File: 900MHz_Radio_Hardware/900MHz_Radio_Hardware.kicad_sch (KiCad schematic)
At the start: 10 parts, among them U1 TSR_1-2450

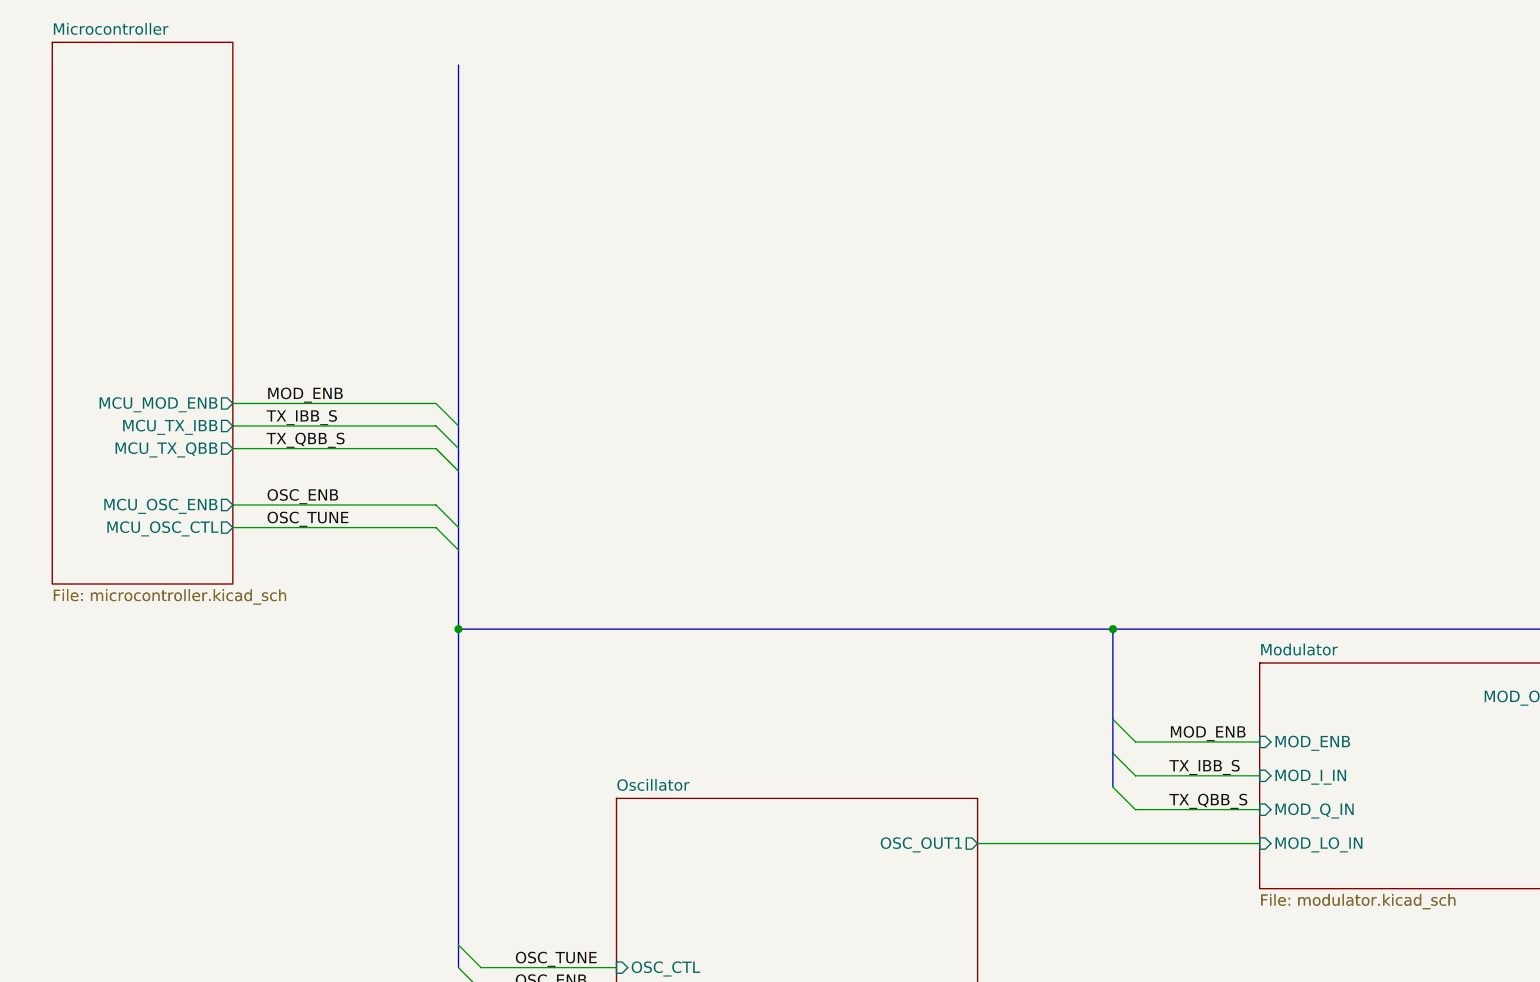
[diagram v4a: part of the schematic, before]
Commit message: Replaced DAC
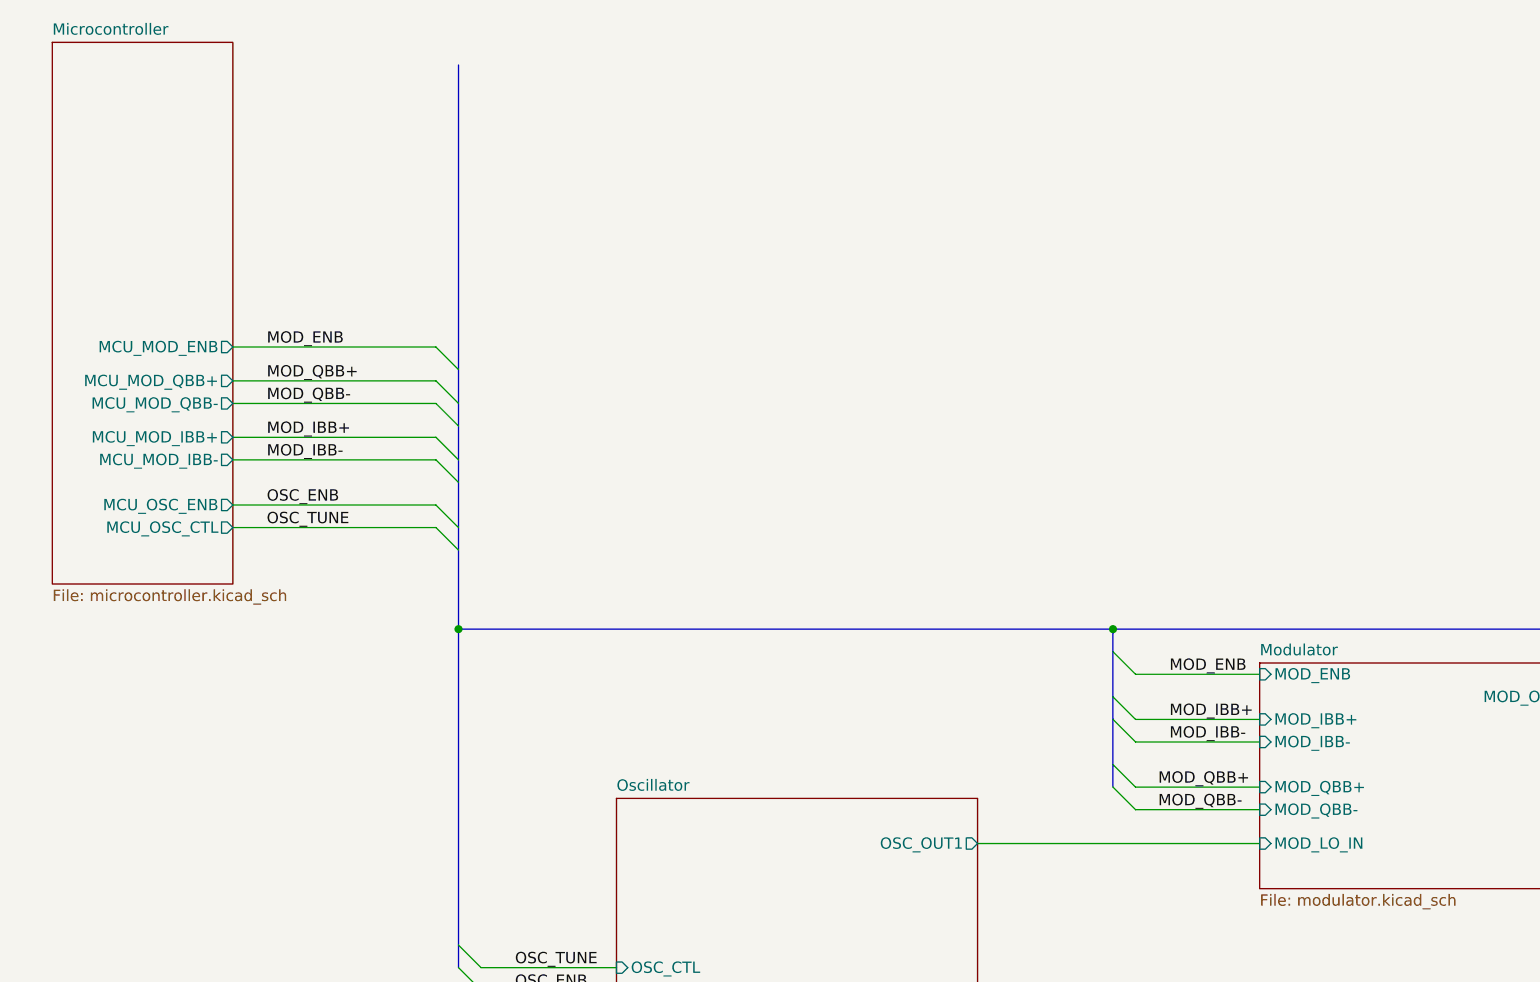
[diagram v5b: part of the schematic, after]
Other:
- sheet Microcontroller ports: added MCU_MOD_IBB+, MCU_MOD_IBB-, MCU_MOD_QBB+, MCU_MOD_QBB-; removed MCU_TX_IBB, MCU_TX_QBB
- sheet Modulator ports: added MOD_IBB+, MOD_IBB-, MOD_QBB+, MOD_QBB-; removed MOD_I_IN, MOD_Q_IN

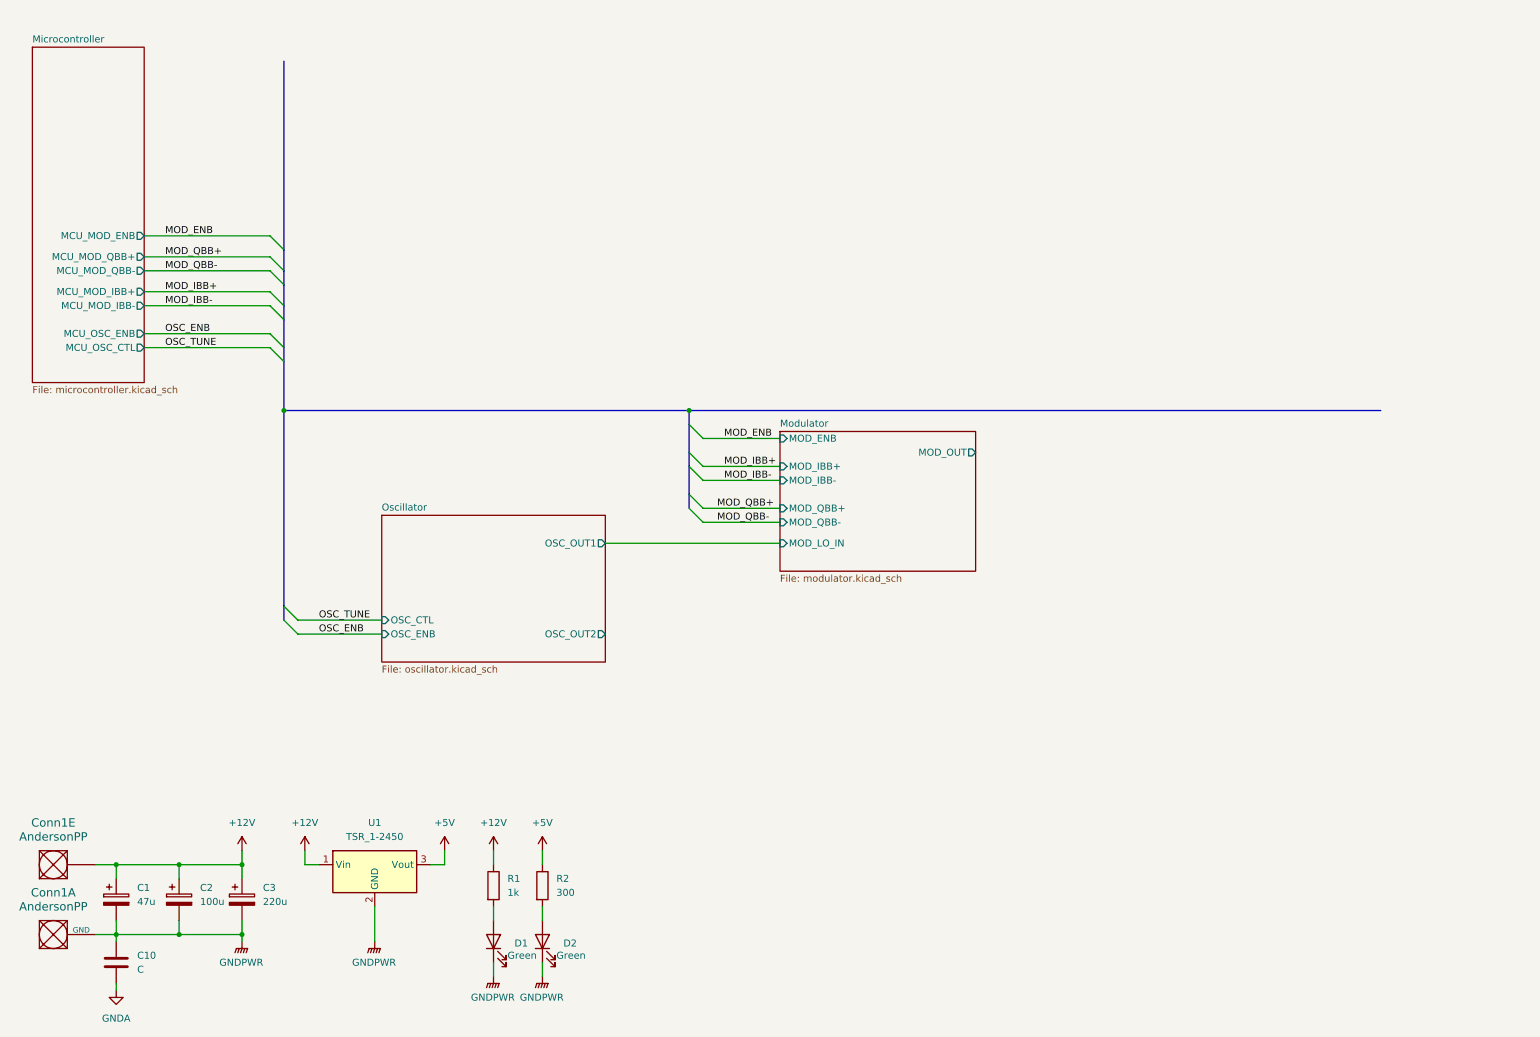
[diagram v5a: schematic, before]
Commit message: Started demodulator
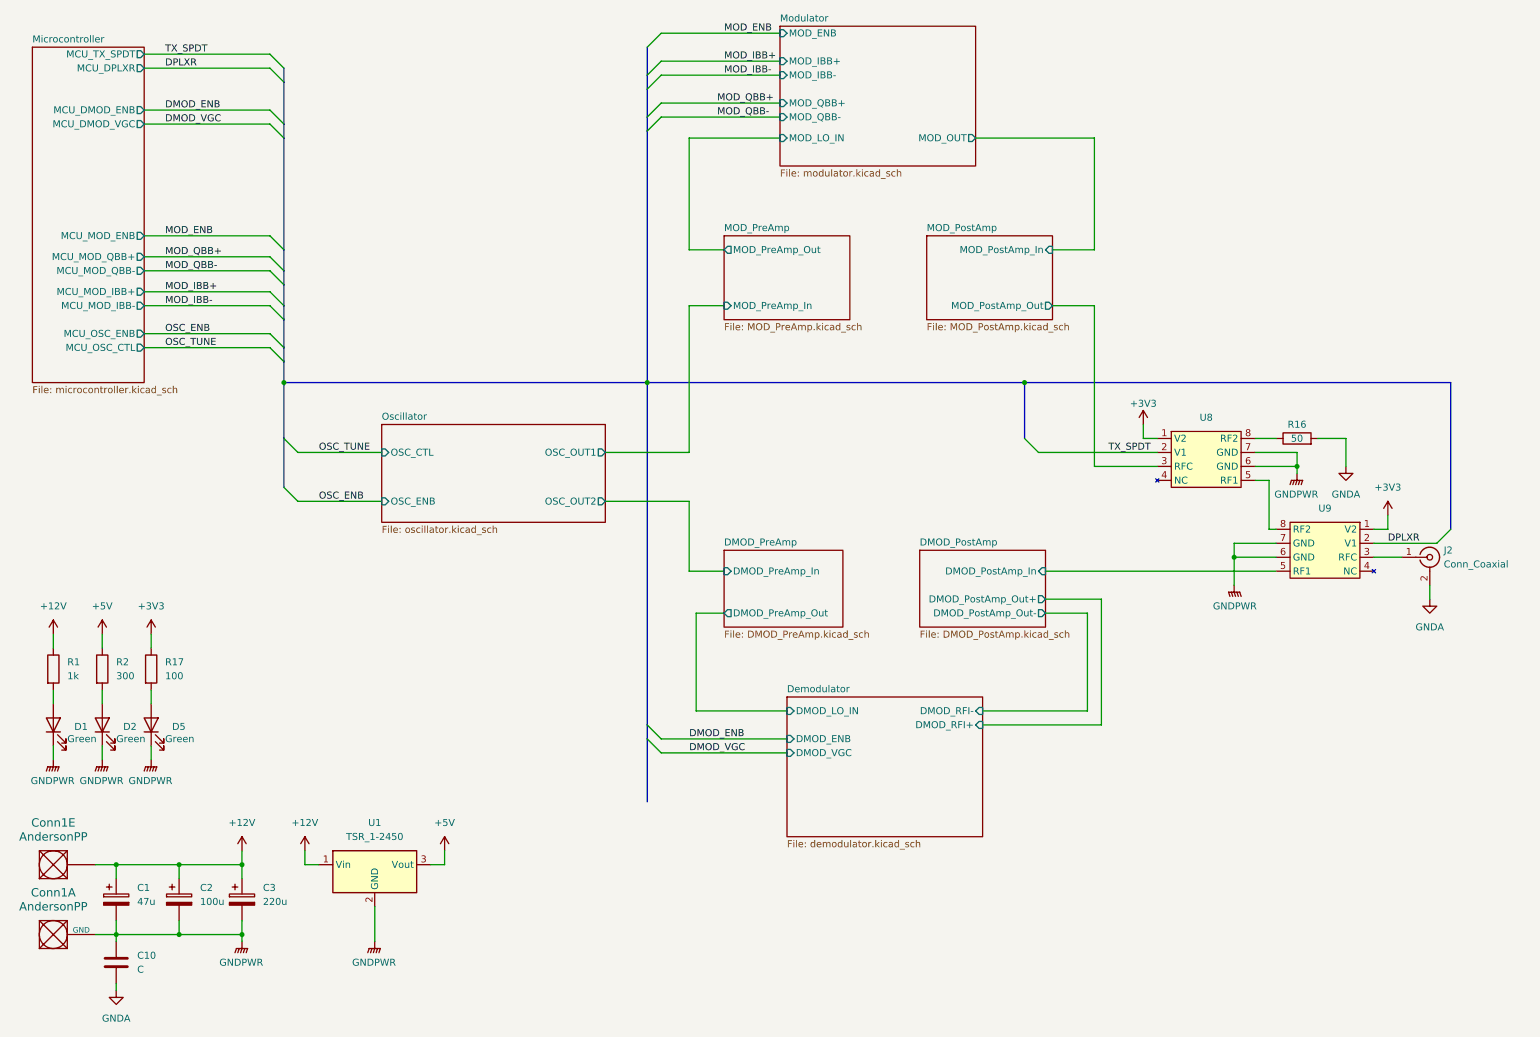
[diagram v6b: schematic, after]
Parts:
- added D5: Green, symbol Device:LED
- added J2: Conn_Coaxial, symbol Connector:Conn_Coaxial
- added R16: 50, symbol Device:R
- added R17: 100, symbol Device:R
- added U8, U9: ~, Package_SO:MSOP-8-1EP_3x3mm_P0.65mm_EP1.73x1.85mm, symbol MRDT_ICs:PE4251
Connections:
- net GNDA: now also J2.2 (Ext), R16.2
- net GNDPWR: now also D5.1 (K), U8.6 (GND), U8.7 (GND), U9.6 (GND), U9.7 (GND)
- new net: D5.2 (A), R17.2
- new net: J2.1 (In), U9.3 (RFC)
- new net: U8.5 (RF1), U9.8 (RF2)
- new net: R16.1, U8.8 (RF2)
- new net +3V3: R17.1, U8.1 (V2), U9.1 (V2)
- new net DMOD_PostAmp/DMOD_PostAmp_In: U9.5 (RF1)
- new net DPLXR: U9.2 (V1)
- new net MOD_PostAmp/MOD_PostAmp_Out: U8.3 (RFC)
- new net TX_SPDT: U8.2 (V1)
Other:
- added sheet DMOD_PostAmp (DMOD_PostAmp.kicad_sch)
- added sheet DMOD_PreAmp (DMOD_PreAmp.kicad_sch)
- added sheet Demodulator (demodulator.kicad_sch)
- added sheet MOD_PostAmp (MOD_PostAmp.kicad_sch)
- added sheet MOD_PreAmp (MOD_PreAmp.kicad_sch)
- sheet Microcontroller ports: added MCU_DMOD_ENB, MCU_DMOD_VGC, MCU_DPLXR, MCU_TX_SPDT; removed none
- moved on the sheet: D1, D2, R1, R2

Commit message: Worked on demodulator
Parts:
- removed C10: C, symbol Device:C
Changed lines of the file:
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@@
-    )
-  )
-  (symbol (lib_id "Device:C") (at 30.48 185.42 0) (unit 1)
-    (in_bom yes) (on_board yes) (dnp no) (fields_autoplaced)
-    (property "Reference" "C10" (at 34.29 184.15 0)
-      (effects (font (size 1.27 1.27)) (justify left))
-    )
-    (property "Value" "C" (at 34.29 186.69 0)
-      (effects (font (size 1.27 1.27)) (justify left))
-    )
-    (property "Footprint" "" (at 31.4452 189.23 0)
-      (effects (font (size 1.27 1.27)) hide)
-    )
-    (property "Datasheet" "~" (at 30.48 185.42 0)
-      (effects (font (size 1.27 1.27)) hide)
-    )
-    (pin "1")
-    (pin "2")
-    (instances
-      (project "900MHz_Radio_Hardware"
-        (path "/8d477a51-3dbb-4c04-84c7-90186d141eda"
-          (reference "C10") (unit 1)
-        )
-      )
     )
   )

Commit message: Renamed amp sheets
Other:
- sheet DMOD_PostAmp renamed DMOD_RF_Amp
- sheet DMOD_PreAmp renamed DMOD_LO_Amp
- sheet MOD_PostAmp renamed MOD_RF_Amp
- sheet MOD_PreAmp renamed MOD_LO_Amp
- sheet DMOD_LO_Amp: file DMOD_PreAmp.kicad_sch -> DMOD_LO_Amp.kicad_sch
- sheet DMOD_RF_Amp: file DMOD_PostAmp.kicad_sch -> DMOD_RF_Amp.kicad_sch
- sheet MOD_LO_Amp: file MOD_PreAmp.kicad_sch -> MOD_LO_Amp.kicad_sch
- sheet MOD_RF_Amp: file MOD_PostAmp.kicad_sch -> MOD_RF_Amp.kicad_sch
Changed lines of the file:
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@@
     (stroke (width 0.1524) (type solid))
     (fill (color 0 0 0 0.0000))
-    (property "Sheetname" "MOD_PostAmp" (at 177.8 52.6284 0)
+    (property "Sheetname" "MOD_RF_Amp" (at 177.8 52.6284 0)
       (effects (font (size 1.27 1.27)) (justify left bottom))
     )
-    (property "Sheetfile" "MOD_PostAmp.kicad_sch" (at 177.8 69.1646 0)
+    (property "Sheetfile" "MOD_RF_Amp.kicad_sch" (at 177.8 69.1646 0)
       (effects (font (size 1.27 1.27)) (justify left top))
     )
@@
     (stroke (width 0.1524) (type solid))
     (fill (color 0 0 0 0.0000))
-    (property "Sheetname" "MOD_PreAmp" (at 140.97 52.6284 0)
+    (property "Sheetname" "MOD_LO_Amp" (at 140.97 52.6284 0)
       (effects (font (size 1.27 1.27)) (justify left bottom))
     )
-    (property "Sheetfile" "MOD_PreAmp.kicad_sch" (at 140.97 69.1646 0)
+    (property "Sheetfile" "MOD_LO_Amp.kicad_sch" (at 140.97 69.1646 0)
       (effects (font (size 1.27 1.27)) (justify left top))
     )
@@
     (stroke (width 0.1524) (type solid))
     (fill (color 0 0 0 0.0000))
-    (property "Sheetname" "DMOD_PostAmp" (at 176.53 109.7784 0)
+    (property "Sheetname" "DMOD_RF_Amp" (at 176.53 109.7784 0)
       (effects (font (size 1.27 1.27)) (justify left bottom))
     )
-    (property "Sheetfile" "DMOD_PostAmp.kicad_sch" (at 176.53 125.0446 0)
+    (property "Sheetfile" "DMOD_RF_Amp.kicad_sch" (at 176.53 125.0446 0)
       (effects (font (size 1.27 1.27)) (justify left top))
     )
@@
     (stroke (width 0.1524) (type solid))
     (fill (color 0 0 0 0.0000))
-    (property "Sheetname" "DMOD_PreAmp" (at 140.97 109.7784 0)
+    (property "Sheetname" "DMOD_LO_Amp" (at 140.97 109.7784 0)
       (effects (font (size 1.27 1.27)) (justify left bottom))
     )
-    (property "Sheetfile" "DMOD_PreAmp.kicad_sch" (at 140.97 125.0446 0)
+    (property "Sheetfile" "DMOD_LO_Amp.kicad_sch" (at 140.97 125.0446 0)
       (effects (font (size 1.27 1.27)) (justify left top))
     )
